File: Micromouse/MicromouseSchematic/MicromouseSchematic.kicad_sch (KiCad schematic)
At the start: 26 parts, among them J3 Conn_01x04_Pin, J4 Conn_01x02_Pin, SW1 SW_Push, SW2 SW_Push, U5 STM32F746VETx, Y1 8MHz, Y2 32.768kHz

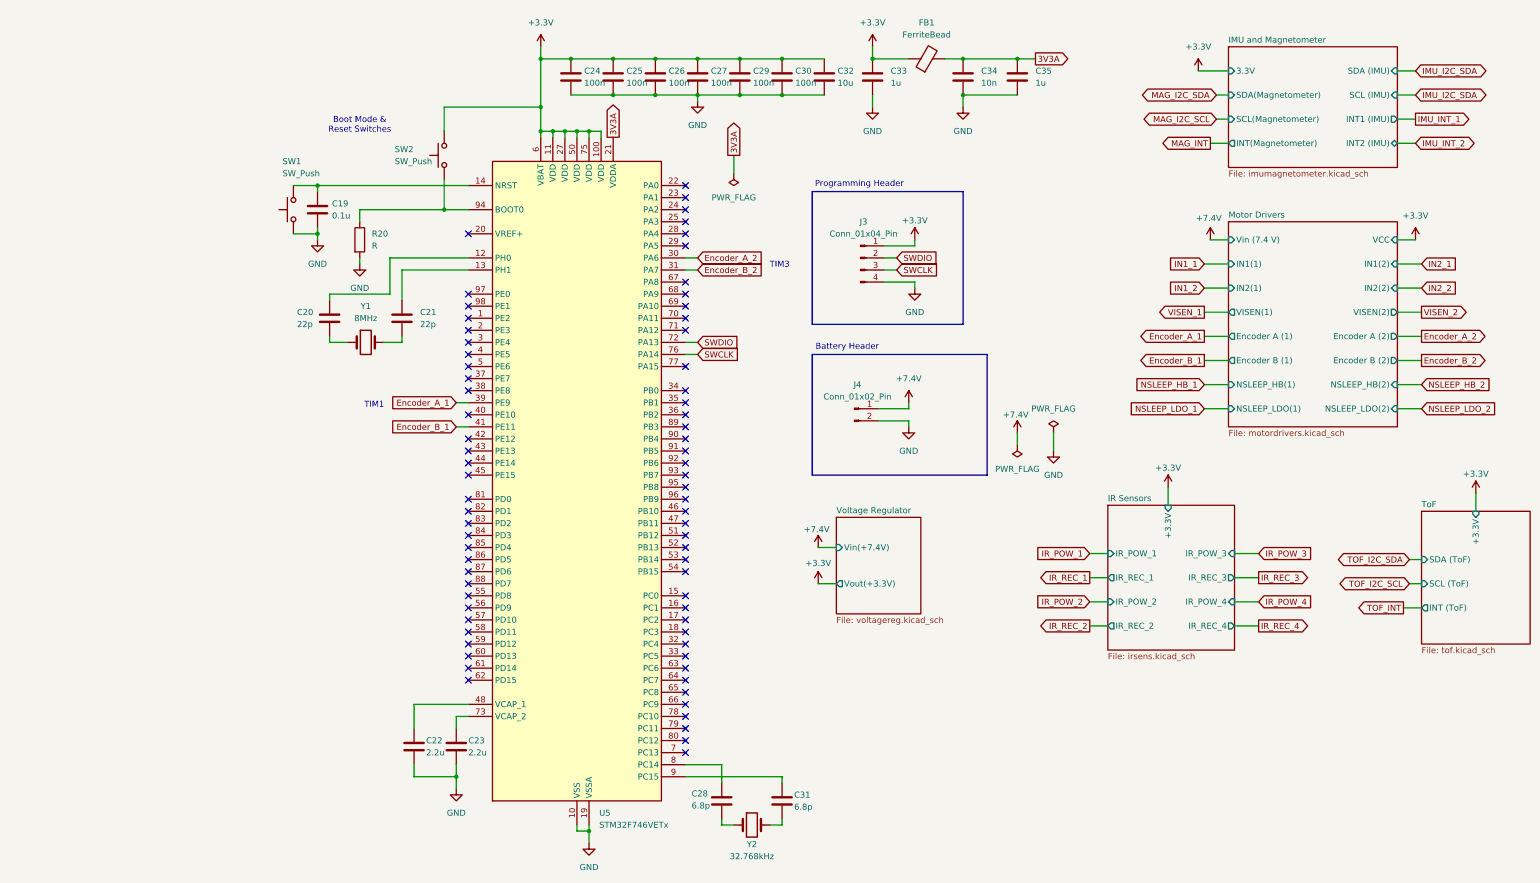
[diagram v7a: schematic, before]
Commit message: Micromouse KiCad: MP6550 libs in project, fp-lib paths, schematic updates
Move MP6550G-Z symbol and legacy footprints into MicromouseSchematic, add
MP6550G-Z.pretty with MP6550_MNP footprint, and point fp-lib-table at the
project-local MM_MP6550G-Z library.

Replace old absolute footprint paths with this repo’s Micromouse tree and
MM_* library names. Update root schematic and IMU/IR/motor/TOF/regulator
subsheets; add empty bluethooth.kicad_sch hierarchical sheet. Extend KiCad
project BOM field configuration; refresh fp-info-cache. Drop schematic lock
file; include dated schematic backup zip.
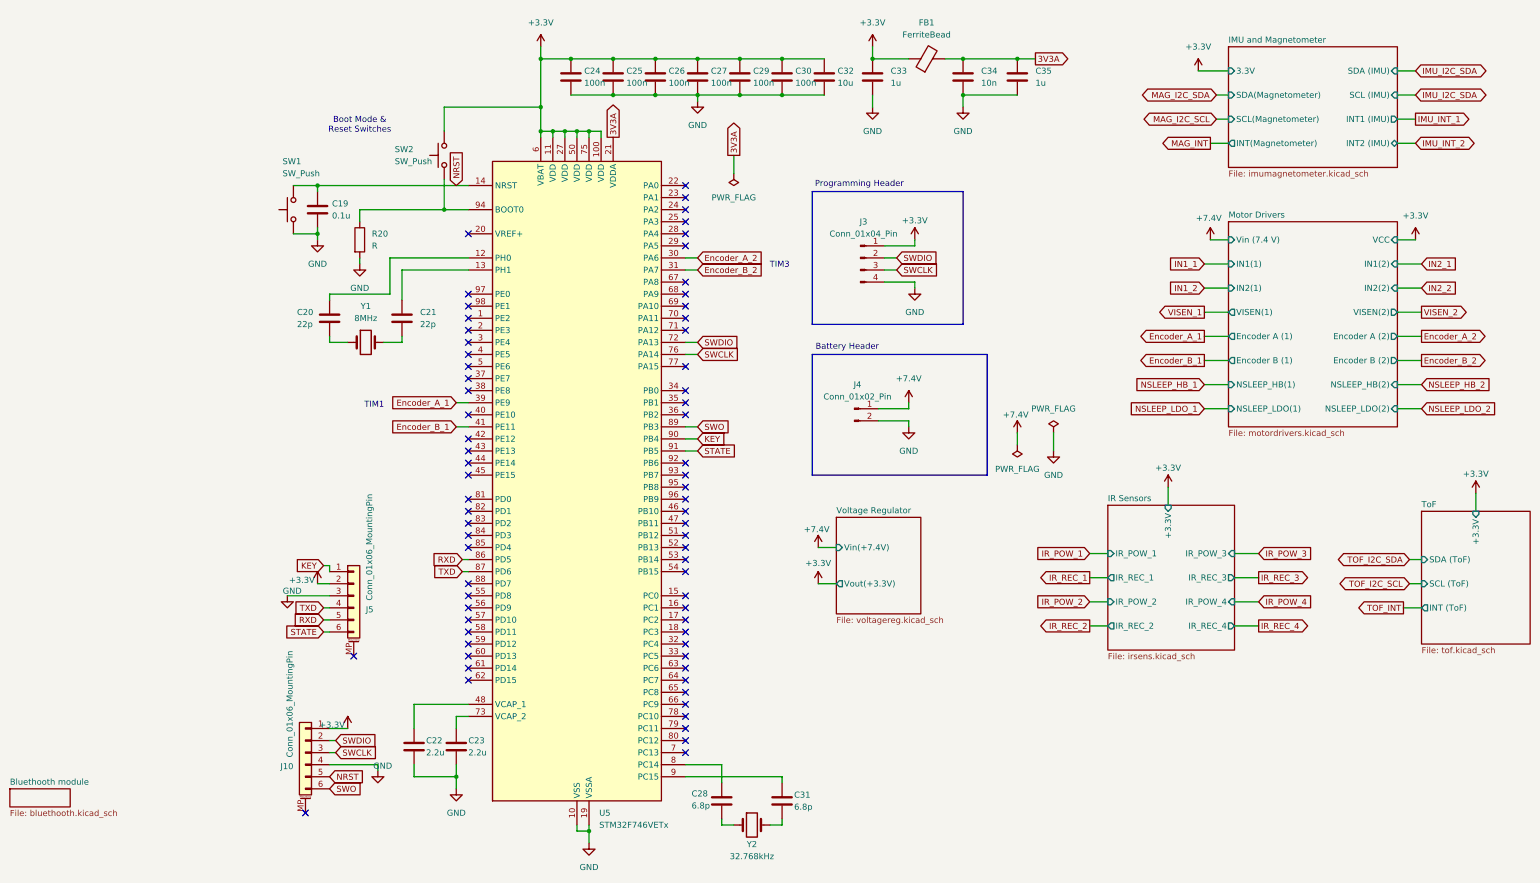
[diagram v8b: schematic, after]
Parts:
- added J10, J5: Conn_01x06_MountingPin, symbol Connector_Generic_MountingPin:Conn_01x06_MountingPin
- J4: footprint (none) -> Connector:CUI_PD-30
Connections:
- net +3.3V: now also J10.1 (Pin_1), J5.2 (Pin_2)
- net GND: now also J10.4 (Pin_4), J5.3 (Pin_3)
- net SWCLK: now also J10.3 (Pin_3)
- net SWDIO: now also J10.2 (Pin_2)
- net NRST: now reaches C19.1, SW1.2, U5.14 (NRST)
- net NRST: now also J10.5 (Pin_5)
- net RXD: now reaches U5.86 (PD5)
- net RXD: now also J5.5 (Pin_5)
- net TXD: now reaches U5.87 (PD6)
- net TXD: now also J5.4 (Pin_4)
- net SWO: now reaches U5.89 (PB3)
- net SWO: now also J10.6 (Pin_6)
- net KEY: now reaches U5.90 (PB4)
- net KEY: now also J5.1 (Pin_1)
- net STATE: now reaches U5.91 (PB5)
- net STATE: now also J5.6 (Pin_6)
- no-connect marks 73 -> 70
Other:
- added sheet Bluethooth module (bluethooth.kicad_sch)
